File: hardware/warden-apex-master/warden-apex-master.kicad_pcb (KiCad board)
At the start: 4 copper layers, 100 x 100 mm, 88 parts, among them IC1 SIM7080G, IC2 BQ24650RVAR, IC3 TPS63070RNMR, IC4 MAX98357AETE+T, J1 U.FL-R-SMT-1, J2 U.FL-R-SMT-1, J3 61300211121, J4 Expansion_Header, J5 Qwiic, Q1 DMG9926UDM, Q2 AO3401A, Q3 2N7002, U1 113991115, U2 Ai-Thinker-Ra-01, U3 M138 Modem, U4 MCP23017_SO, U5 SRV05-4-P-T7, U6 SC16IS740, X1 14.7456MHz

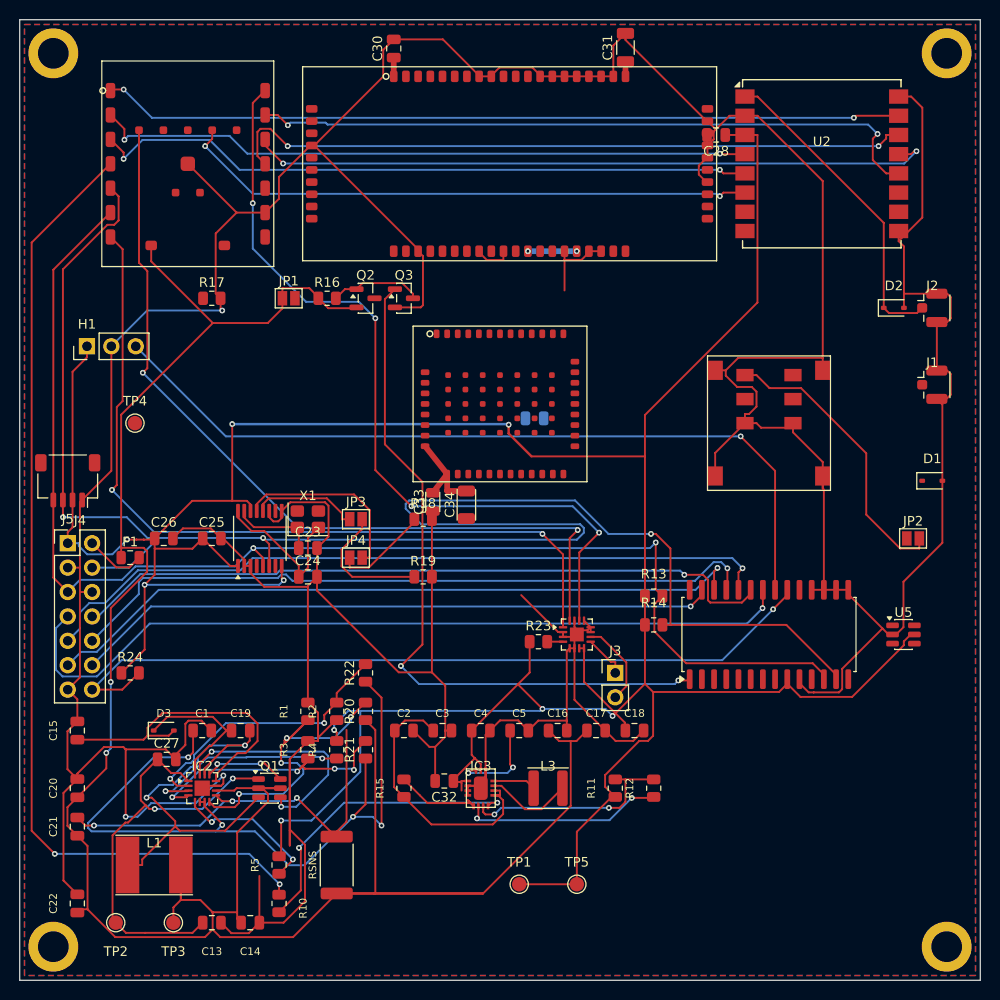
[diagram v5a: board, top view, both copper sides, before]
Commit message: Update warden-apex design for Phase 22 power-rail hardening. Enhanced README.md with detailed changes, including widened power-net segments and added ground stitching. Updated Gerber files with new timestamps and corrected net connections. Added new entries to .gitignore for build artifacts and prompt files.
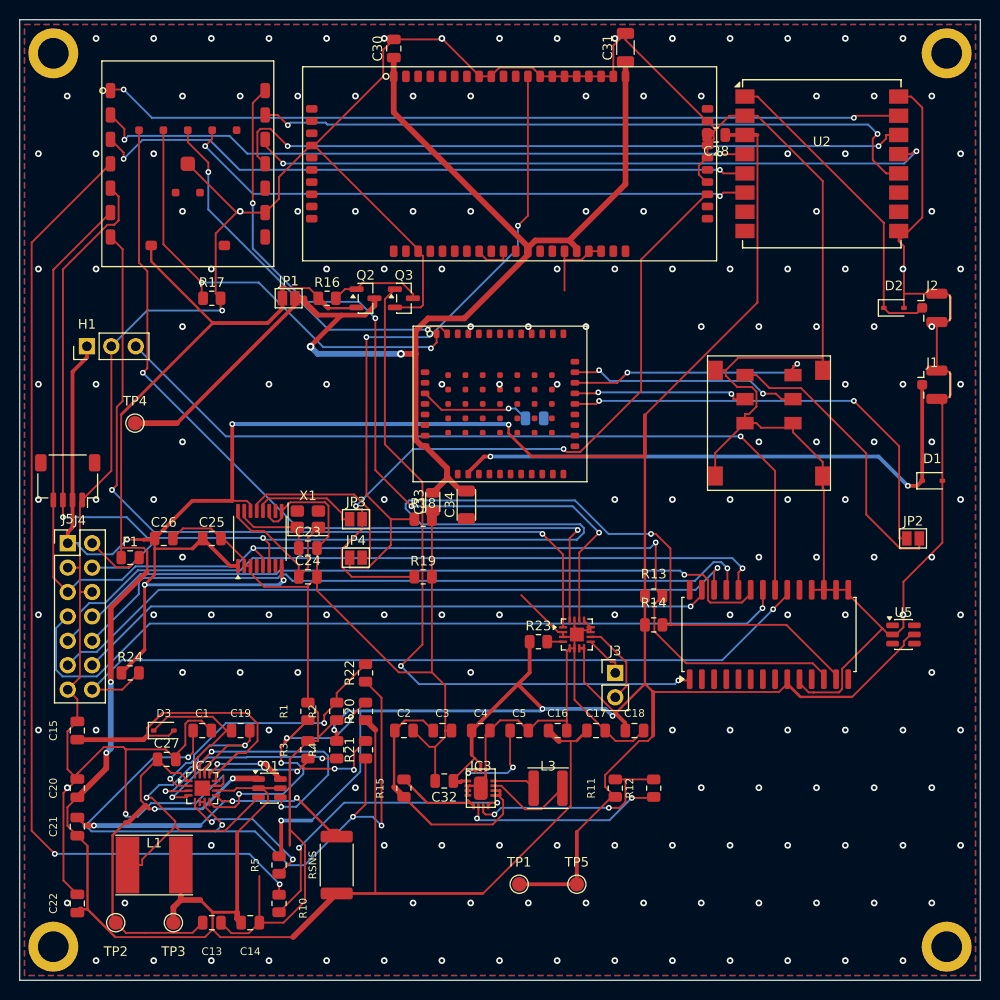
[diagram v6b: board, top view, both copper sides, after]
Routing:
- net /MODEM_VBAT_SW: track 18.5 -> 139.2 mm
- net /UART2_TX: track 13.8 -> 74.0 mm, vias 0 -> 2
- net /CELL_RF: track 0.00 -> 59.6 mm, vias 0 -> 2
- net /UART2_RX: track 10.1 -> 69.4 mm, vias 0 -> 2
- net /UART1_RX: track 0.00 -> 47.7 mm, vias 0 -> 2
- net /SIM_VDD: track 0.00 -> 46.2 mm, vias 0 -> 2
- net /3V3: track 361.5 -> 404.5 mm
- net /UART1_TX: track 0.00 -> 39.7 mm, vias 0 -> 2
- net /SIM_CLK: track 0.00 -> 25.5 mm, vias 0 -> 2
- net /SIM_DATA: track 0.00 -> 24.0 mm, vias 0 -> 2
- net /SIM_RST: track 0.00 -> 18.2 mm, vias 0 -> 2
- net /SIM_VDD_EXT: track 0.00 -> 11.6 mm, vias 0 -> 1
- net /CHG_SENSE_NEG: track 43.5 -> 32.5 mm
- net /REG_EN: track 9.67 -> 13.1 mm
- net /GND: vias 3 -> 173

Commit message: Refine warden-apex design by removing unused components C35, C36, and R25 from BOM files. Update README.md to reflect UART1 routing changes, now directly connecting between U1 and IC1. Revise Gerber files with new timestamps and ensure consistency across documentation. Clean up schematic with follow-on parity adjustments, resulting in zero schematic-parity warnings.
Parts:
- C31: footprint C_1206_3216Metric -> Capacitor_SMD:C_1206_3216Metric
- F1: footprint Fuse_0805_2012Metric -> Fuse:Fuse_0805_2012Metric
- J4: footprint PinHeader_2x07_P2.54mm_Vertical -> Connector_PinHeader_2.54mm:PinHeader_2x07_P2.54mm_Vertical
- J5: footprint JST_SH_SM04B-SRSS-TB_1x04-1MP_P1.00mm_Horizontal -> Connector_JST:JST_SH_SM04B-SRSS-TB_1x04-1MP_P1.00mm_Horizontal
- R24: footprint R_0805_2012Metric -> Resistor_SMD:R_0805_2012Metric
